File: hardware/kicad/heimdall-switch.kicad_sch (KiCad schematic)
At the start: 39 parts, among them J1 SWD, J2 LOAD_OUT, J3 BATT_IN, J4 UI_BREAKOUT, Q1 AO3400A, Q2 BSS84, Q3 AO4407A, Q4 AO4407A, Q5 AO3400A, SW1 KSC221J, U1 BT832, U2 TPS629206, Y1 32.768kHz

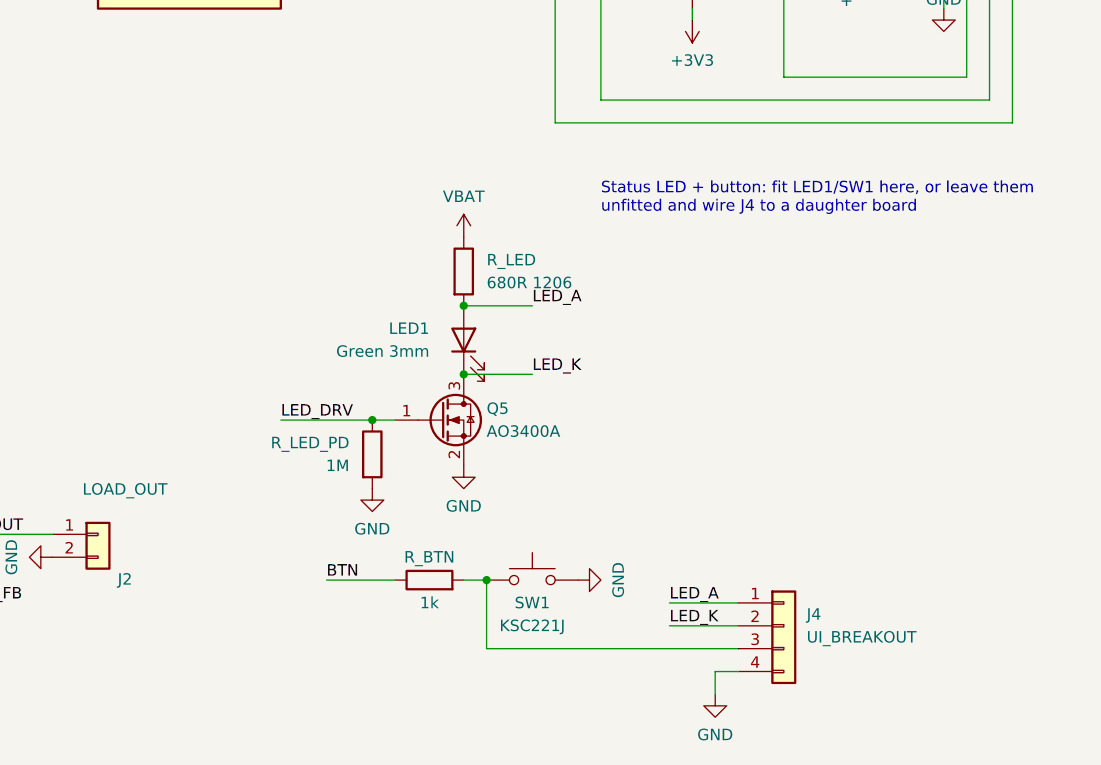
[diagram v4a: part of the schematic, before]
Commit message: Status LED: high-side switch so the daughter board needs 3 wires
Q6 (BSS84) now switches VBAT into R_LED/LED1 from the high side, driven
by Q5 (AO3400A) with R_Q6_PU 1M; the LED cathode goes straight to GND.
J4 is back to 3 pads: LED_A / BTN / GND, the LED and button sharing
the ground wire. R_LED stays ahead of J4, so a shorted daughter-board
wire is still current-limited.

Co-Authored-By: Claude Opus 5.5 <noreply@anthropic.com>
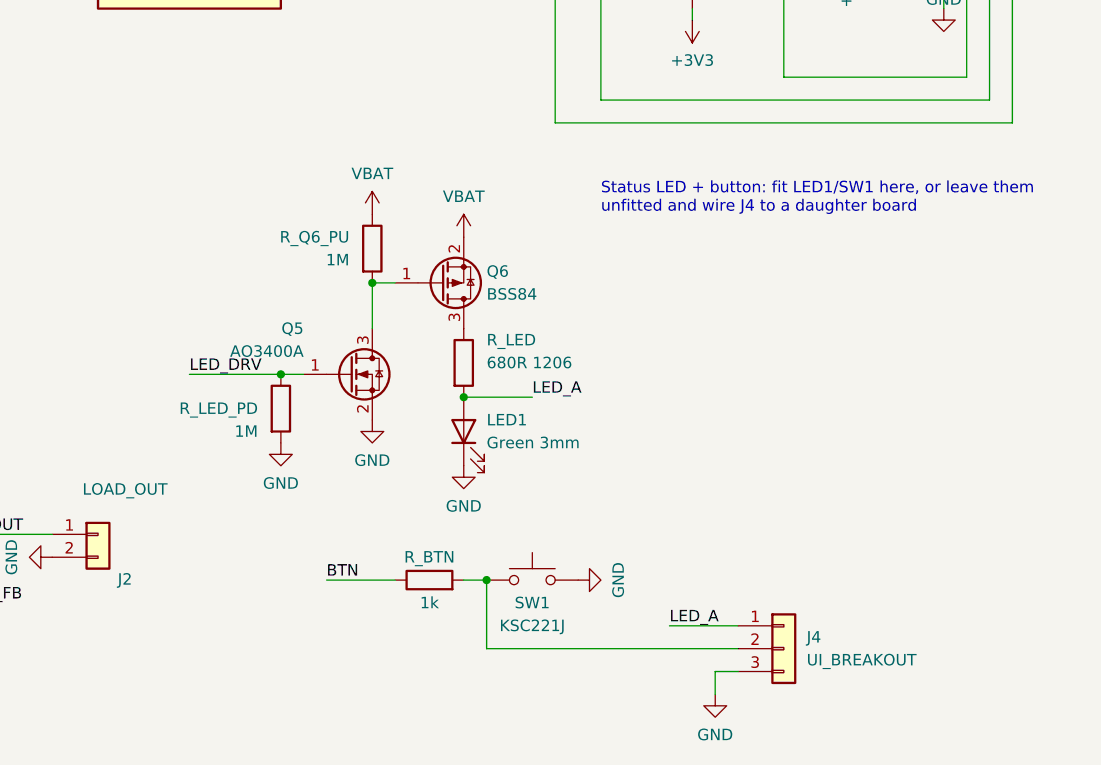
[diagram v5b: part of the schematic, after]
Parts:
- removed J4: UI_BREAKOUT, symbol Connector_Generic:Conn_01x04
- added J4: UI_BREAKOUT, symbol Connector_Generic:Conn_01x03
- added Q6: BSS84, symbol Transistor_FET:Q_PMOS_GSD
- added R_Q6_PU: 1M, symbol Device:R
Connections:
- net GND: now also LED1.1 (K), J4.3 (Pin_3)
- net LED_A: now also J4.1 (Pin_1)
- net VBAT: now also Q6.2 (S), R_Q6_PU.1; no longer R_LED.1
- net at R_BTN.2, SW1.1: now also J4.2 (Pin_2)
- net LED_K: no longer names the net of Q5.3 (D)
- net LED_K: now also Q6.1 (G), R_Q6_PU.2; no longer LED1.1 (K)
- new net: Q6.3 (D), R_LED.1

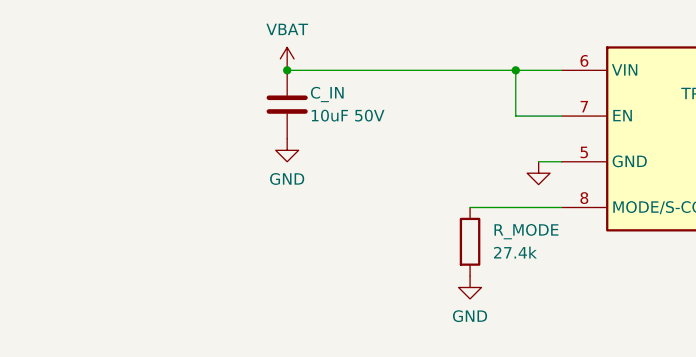
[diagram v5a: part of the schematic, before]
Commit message: Add R_IN hot-plug damping in front of the regulator
Plugging a 3S pack into ceramic-only input capacitance rings up to ~2x
pack voltage, past the TPS629206's 17V rating. A bulk electrolytic
would be bigger than the board, so R_IN (22R 0603) now sits between
VBAT and C_IN/U2: heavily overdamped, caps inrush at ~0.6A, and drops
<=0.1V at the regulator's mA-level draw. The load path is unaffected.

Co-Authored-By: Claude Opus 5.5 <noreply@anthropic.com>
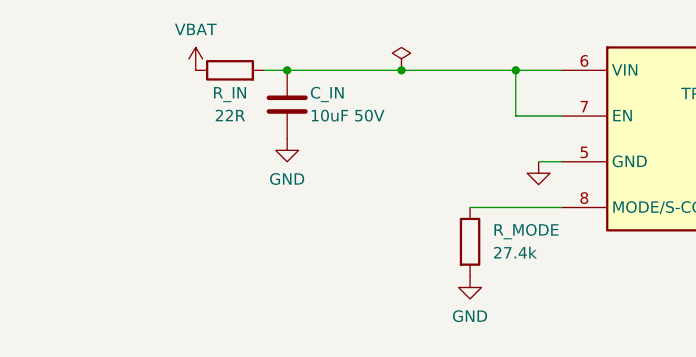
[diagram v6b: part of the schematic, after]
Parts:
- added R_IN: 22R, symbol Device:R
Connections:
- net VBAT: now also R_IN.1; no longer C_IN.1, U2.6 (VIN), U2.7 (EN)
- new net: C_IN.1, R_IN.2, U2.6 (VIN), U2.7 (EN)
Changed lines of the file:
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@@
 	)
 	(junction
+		(at 58.42 48.26)
+		(diameter 0)
+		(color 0 0 0 0)
+	)
+	(junction
 		(at 142.24 175.26)
 		(diameter 0)
@@
 	(wire
 		(pts
+			(xy 43.18 48.26) (xy 45.72 48.26)
+		)
+		(stroke
+			(width 0)
+			(type default)
+		)
+	)
+	(wire
+		(pts
 			(xy 195.58 76.2) (xy 236.22 76.2)
 		)
@@
 	)
 	(symbol
-		(lib_id "power:+BATT")
-		(at 45.72 48.26 0)
-		(unit 1)
-		(body_style 1)
-		(exclude_from_sim no)
-		(in_bom yes)
-		(on_board yes)
-		(in_pos_files yes)
-		(dnp no)
-		(property "Reference" "#PWR41"
-			(at 45.72 48.26 0)
-			(hide yes)
-			(show_name no)
-			(do_not_autoplace no)
-			(effects
-				(font
-					(size 1.27 1.27)
-				)
-			)
-		)
-		(property "Value" "VBAT"
-			(at 45.72 43.76 0)
-			(show_name no)
-			(do_not_autoplace no)
-			(effects
-				(font
-					(size 1.27 1.27)
-				)
-			)
-		)
-		(property "Footprint" ""
-			(at 45.72 48.26 0)
-			(hide yes)
-			(show_name no)
-			(do_not_autoplace no)
-			(effects
-				(font
-					(size 1.27 1.27)
-				)
-			)
-		)
-		(property "Datasheet" ""
-			(at 45.72 48.26 0)
-			(hide yes)
-			(show_name no)
-			(do_not_autoplace no)
-			(effects
-				(font
-					(size 1.27 1.27)
-				)
-			)
-		)
-		(property "Description" ""
-			(at 45.72 48.26 0)
-			(show_name no)
-			(do_not_autoplace no)
-			(effects
-				(font
-					(size 1.27 1.27)
-				)
-			)
-		)
-		(pin "1"
-		)
-		(instances
-			(project "heimdall-switch"
-				(path "/661790ab-8e2f-4c6b-b033-e8b244002c23"
-					(reference "#PWR41")
-					(unit 1)
-				)
-			)
-		)
-	)
-	(symbol
 		(lib_id "power:GND")
 		(at 40.64 104.14 0)
@@
 	(symbol
 		(lib_id "Device:R")
+		(at 39.37 48.26 90)
+		(unit 1)
+		(body_style 1)
+		(exclude_from_sim no)
+		(in_bom yes)
+		(on_board yes)
+		(in_pos_files yes)
+		(dnp no)
+		(property "Reference" "R_IN"
+			(at 39.37 50.8 90)
+			(show_name no)
+			(do_not_autoplace no)
+			(effects
+				(font
+					(size 1.27 1.27)
+				)
+			)
+		)
+		(property "Value" "22R"
+			(at 39.37 53.34 90)
+			(show_name no)
+			(do_not_autoplace no)
+			(effects
+				(font
+					(size 1.27 1.27)
+				)
+			)
+		)
+		(property "Footprint" ""
+			(at 39.37 48.26 0)
+			(hide yes)
+			(show_name no)
+			(do_not_autoplace no)
+			(effects
+				(font
+					(size 1.27 1.27)
+				)
+			)
+		)
+		(property "Datasheet" ""
+			(at 39.37 48.26 0)
+			(hide yes)
+			(show_name no)
+			(do_not_autoplace no)
+			(effects
+				(font
+					(size 1.27 1.27)
+				)
+			)
+		)
+		(property "Description" ""
+			(at 39.37 48.26 0)
+			(show_name no)
+			(do_not_autoplace no)
+			(effects
+				(font
+					(size 1.27 1.27)
+				)
+			)
+		)
+		(property "LCSC" "C23345"
+			(at 39.37 48.26 0)
+			(hide yes)
+			(show_name no)
+			(do_not_autoplace no)
+			(effects
+				(font
+					(size 1.27 1.27)
+				)
+			)
+		)
+		(pin "1"
+		)
+		(pin "2"
+		)
+		(instances
+			(project "heimdall-switch"
+				(path "/661790ab-8e2f-4c6b-b033-e8b244002c23"
+					(reference "R_IN")
+					(unit 1)
+				)
+			)
+		)
+	)
+	(symbol
+		(lib_id "Device:R")
 		(at 99.06 158.75 0)
 		(unit 1)
@@
 	)
 	(symbol
+		(lib_id "power:+BATT")
+		(at 35.56 48.26 0)
+		(unit 1)
+		(body_style 1)
+		(exclude_from_sim no)
+		(in_bom yes)
+		(on_board yes)
+		(in_pos_files yes)
+		(dnp no)
+		(property "Reference" "#PWR101"
+			(at 35.56 48.26 0)
+			(hide yes)
+			(show_name no)
+			(do_not_autoplace no)
+			(effects
+				(font
+					(size 1.27 1.27)
+				)
+			)
+		)
+		(property "Value" "VBAT"
+			(at 35.56 43.76 0)
+			(show_name no)
+			(do_not_autoplace no)
+			(effects
+				(font
+					(size 1.27 1.27)
+				)
+			)
+		)
+		(property "Footprint" ""
+			(at 35.56 48.26 0)
+			(hide yes)
+			(show_name no)
+			(do_not_autoplace no)
+			(effects
+				(font
+					(size 1.27 1.27)
+				)
+			)
+		)
+		(property "Datasheet" ""
+			(at 35.56 48.26 0)
+			(hide yes)
+			(show_name no)
+			(do_not_autoplace no)
+			(effects
+				(font
+					(size 1.27 1.27)
+				)
+			)
+		)
+		(property "Description" ""
+			(at 35.56 48.26 0)
+			(show_name no)
+			(do_not_autoplace no)
+			(effects
+				(font
+					(size 1.27 1.27)
+				)
+			)
+		)
+		(pin "1"
+		)
+		(instances
+			(project "heimdall-switch"
+				(path "/661790ab-8e2f-4c6b-b033-e8b244002c23"
+					(reference "#PWR101")
+					(unit 1)
+				)
+			)
+		)
+	)
+	(symbol
 		(lib_id "Device:C")
 		(at 45.72 52.07 0)
@@
 					(unit 1)
 				)
+			)
+		)
+	)
+	(symbol
+		(lib_id "power:PWR_FLAG")
+		(at 58.42 48.26 0)
+		(unit 1)
+		(body_style 1)
+		(exclude_from_sim no)
+		(in_bom yes)
+		(on_board yes)
+		(in_pos_files yes)
+		(dnp no)
+		(property "Reference" "#FLG13"
+			(at 58.42 48.26 0)
+			(hide yes)
+			(show_name no)
+			(do_not_autoplace no)
+			(effects
+				(font
+					(size 1.27 1.27)
+				)
+			)
+		)
+		(property "Value" "PWR_FLAG"
+			(at 58.42 48.26 0)
+			(hide yes)
+			(show_name no)
+			(do_not_autoplace no)
+			(effects
+				(font
+					(size 1.27 1.27)
+				)
+			)
+		)
+		(property "Footprint" ""
+			(at 58.42 48.26 0)
+			(hide yes)
+			(show_name no)
+			(do_not_autoplace no)
+			(effects
+				(font
+					(size 1.27 1.27)
+				)
+			)
+		)
+		(property "Datasheet" ""
+			(at 58.42 48.26 0)
+			(hide yes)
+			(show_name no)
+			(do_not_autoplace no)
+			(effects
+				(font
+					(size 1.27 1.27)
+				)
+			)
+		)
+		(property "Description" ""
+			(at 58.42 48.26 0)
+			(show_name no)
+			(do_not_autoplace no)
+			(effects
+				(font
+					(size 1.27 1.27)
+				)
+			)
+		)
+		(pin "1"
+		)
+		(instances
+			(project "heimdall-switch"
+				(path "/661790ab-8e2f-4c6b-b033-e8b244002c23"
+					(reference "#FLG13")
+					(unit 1)
+				)

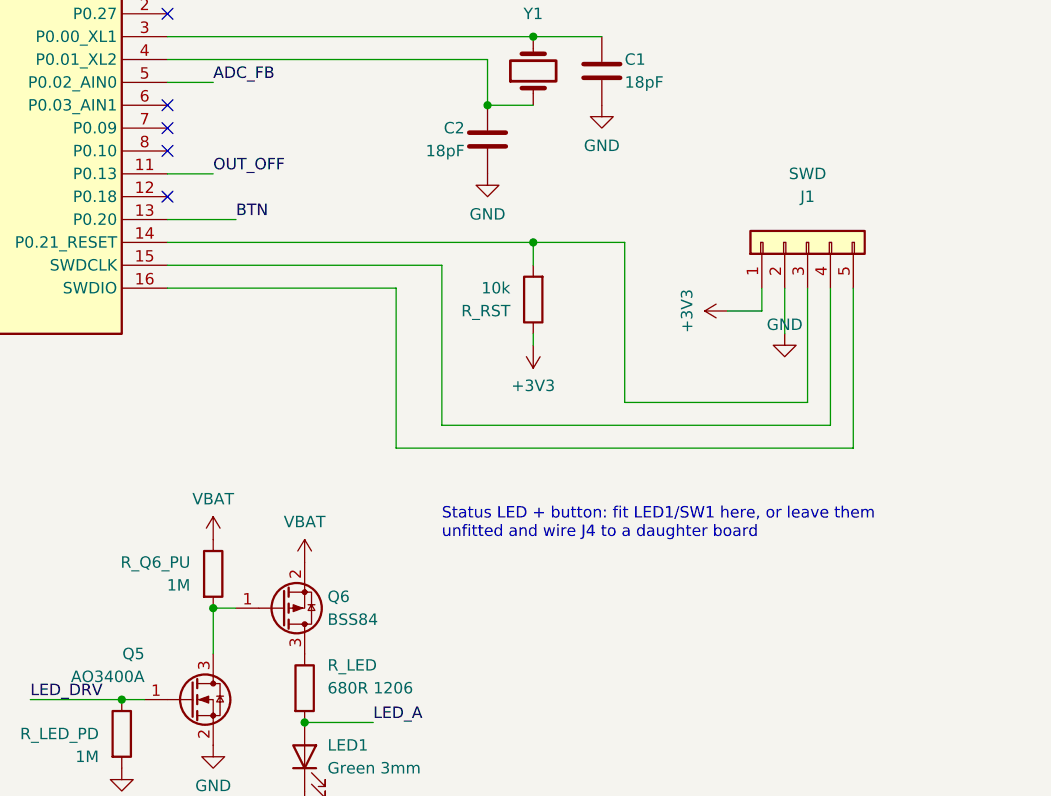
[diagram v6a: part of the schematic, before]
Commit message: J1: standard ARM Cortex Debug 10-pin header, add SWO
J1 is now the 2x5 1.27mm ARM debug connector (Samtec FTSH-105-01-L-DV-K,
male on the board) so J-Link/ST-Link/CMSIS-DAP probes plug straight in.
SWO wired to P0.18 (the nRF52832's fixed trace pin, previously spare).
J1 and R_RST moved to their own block, linked to U1 by net labels.

Co-Authored-By: Claude Opus 5.5 <noreply@anthropic.com>
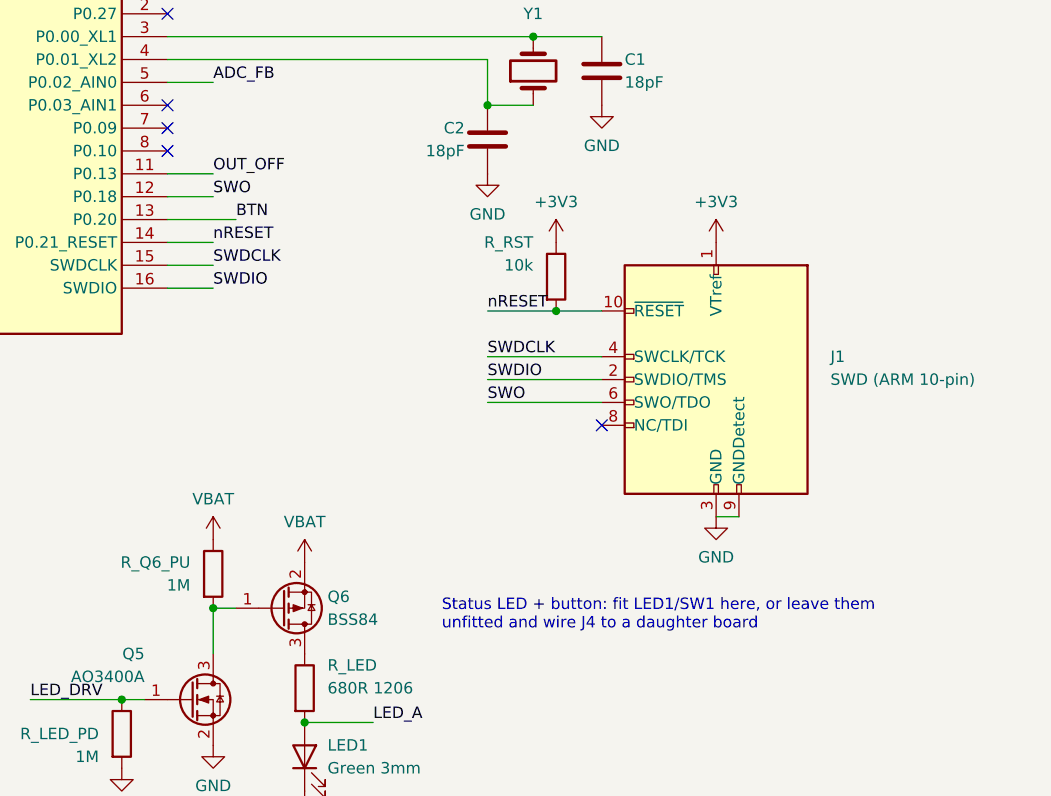
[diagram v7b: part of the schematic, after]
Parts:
- removed J1: SWD, symbol Connector_Generic:Conn_01x05
- added J1: SWD (ARM 10-pin), symbol Connector:Conn_ARM_JTAG_SWD_10
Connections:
- net +3V3: now also J1.1 (VTref)
- net GND: now also J1.3 (GND), J1.5 (GND), J1.9 (GNDDetect)
- net SWO: now reaches U1.12 (P0.18)
- net SWO: now also J1.6 (SWO/TDO)
- net nRESET: now reaches R_RST.2, U1.14 (P0.21_RESET)
- net nRESET: now also J1.10 (~{RESET})
- net SWDCLK: now reaches U1.15 (SWDCLK)
- net SWDCLK: now also J1.4 (SWCLK/TCK)
- net SWDIO: now reaches U1.16 (SWDIO)
- net SWDIO: now also J1.2 (SWDIO/TMS)
